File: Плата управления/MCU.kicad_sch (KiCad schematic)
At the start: 1 part, among them U5 STM32F071V8Tx

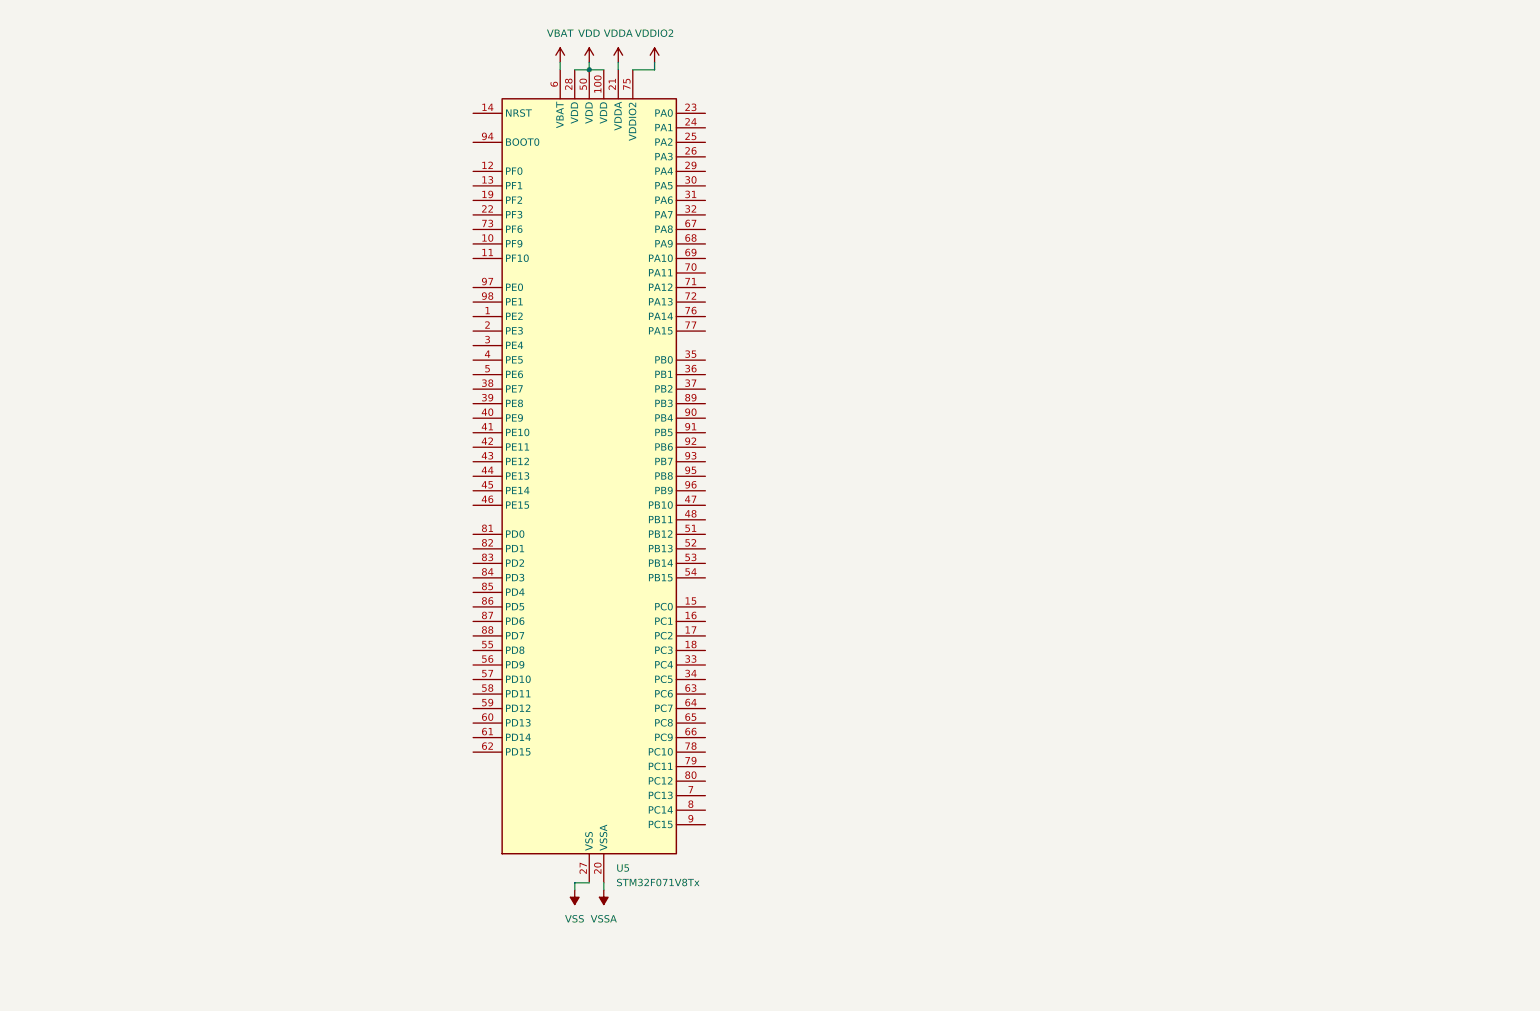
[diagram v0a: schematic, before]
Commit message: Добавил питание MCU и кварц на 8Мгц
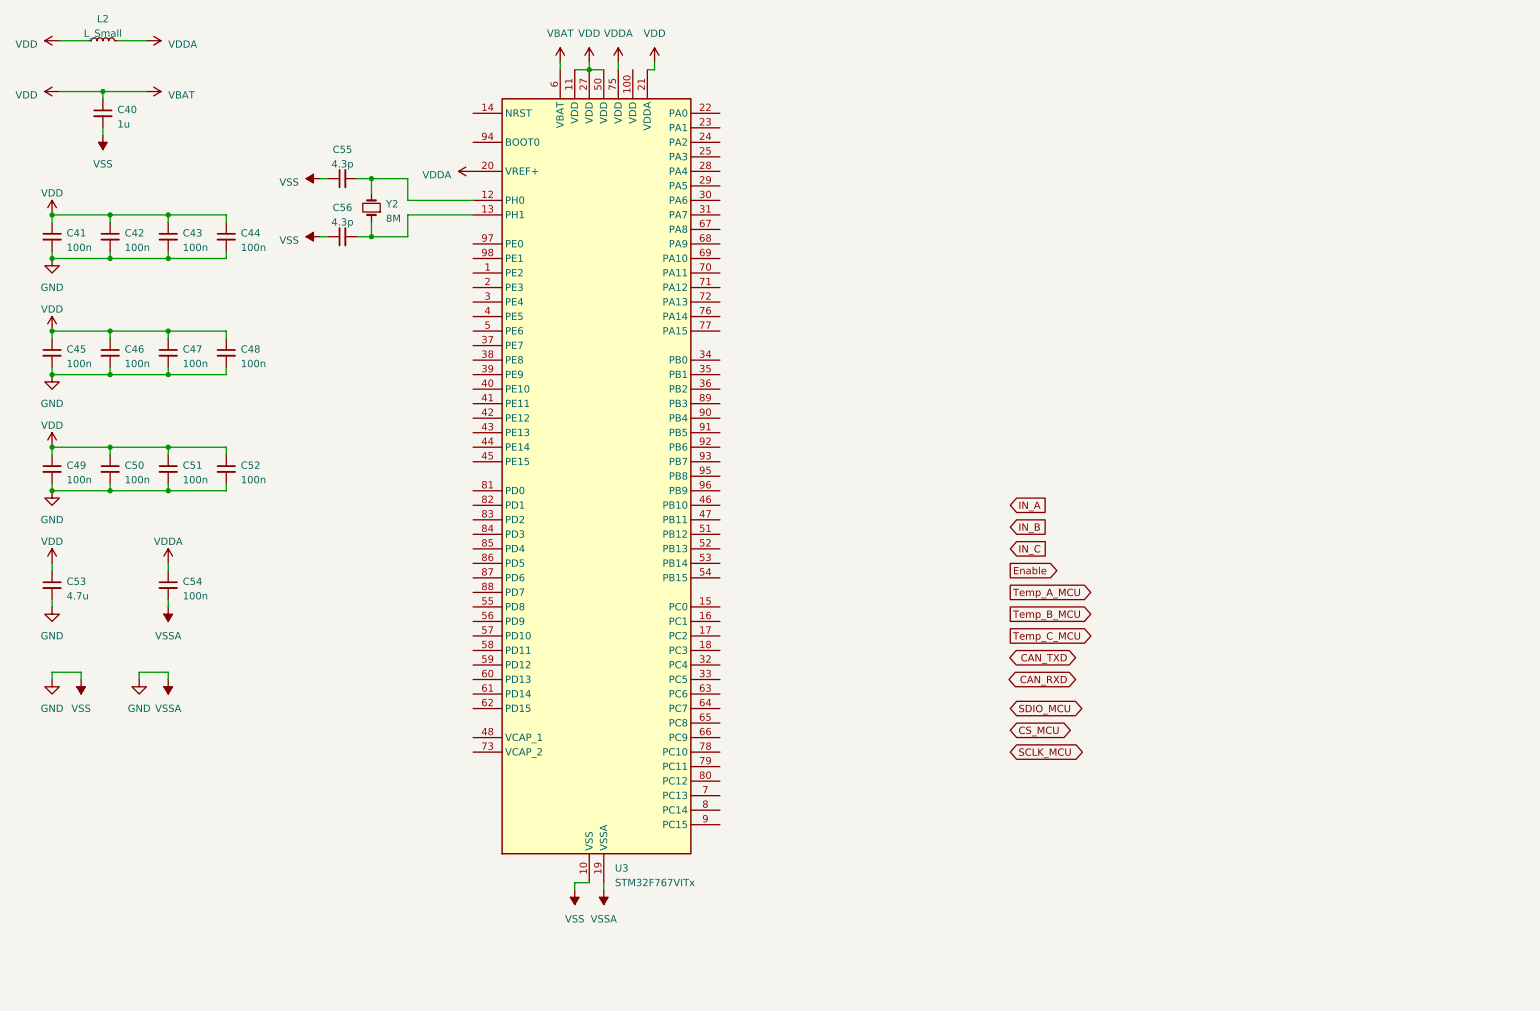
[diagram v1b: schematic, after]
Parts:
- removed U5: STM32F071V8Tx, Package_QFP:LQFP-100_14x14mm_P0.5mm, symbol MCU_ST_STM32F0:STM32F071V8Tx
- added C40: 1u, Capacitor_SMD:C_0603_1608Metric_Pad1.08x0.95mm_HandSolder, symbol Device:C_Small
- added C41, C42, C43, C44, C45, C46, C47, C48, C49, C50, C51, C52, C54: 100n, Capacitor_SMD:C_0603_1608Metric_Pad1.08x0.95mm_HandSolder, symbol Device:C_Small
- added C53: 4.7u, Capacitor_SMD:C_0603_1608Metric_Pad1.08x0.95mm_HandSolder, symbol Device:C_Small
- added C55, C56: 4.3p, Capacitor_SMD:C_0603_1608Metric_Pad1.08x0.95mm_HandSolder, symbol Device:C_Small
- added L2: L_Small, symbol Device:L_Small
- added U3: STM32F767VITx, Package_QFP:LQFP-100_14x14mm_P0.5mm, symbol MCU_ST_STM32F7:STM32F767VITx
- added Y2: 8M, symbol Device:Crystal_Small
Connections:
- net VDD: now also C40.1, C41.1, C42.1, C43.1, C44.1, C45.1, C46.1, C47.1, C48.1, C49.1, C50.1, C51.1, C52.1, C53.1, L2.1, U3.11 (VDD), U3.21 (VDDA), U3.27 (VDD), U3.50 (VDD), U3.6 (VBAT)
- net VDDA: now also C54.1, L2.2, U3.20 (VREF+), U3.75 (VDD)
- new net: C55.2, U3.12 (PH0), Y2.2
- new net: C56.2, U3.13 (PH1), Y2.1
- new net GND: C40.2, C41.2, C42.2, C43.2, C44.2, C45.2, C46.2, C47.2, C48.2, C49.2, C50.2, C51.2, C52.2, C53.2, C54.2, C55.1, C56.1, U3.10 (VSS), U3.19 (VSSA), U3.26 (VSS), U3.49 (VSS), U3.74 (VSS), U3.99 (VSS)

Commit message: Привел в порядок схему
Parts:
- Y1: renamed from Y2; footprint (none) -> Crystal:Crystal_SMD_MicroCrystal_CC1V-T1A-2Pin_8.0x3.7mm
- renumbered C55 to C19, C56 to C20, C41 to C21, C45 to C22, C49 to C23, C53 to C24, C40 to C25, C42 to C26, C46 to C27, C50 to C28, C43 to C29, C47 to C30, C51 to C31, C54 to C32, C44 to C33, C48 to C34, C52 to C35, L2 to L1, U3 to U4
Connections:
- net VDD renamed +3.3V
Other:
- moved on the sheet: C19, C20, C21, C22, C23, C24, C25, C26, C27, C28, C29, C30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

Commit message: Расставил драйвера
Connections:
- net +3.3V: now also U4.100 (VDD)
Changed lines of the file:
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@@
   (junction (at 242.57 69.85) (diameter 0) (color 0 0 0 0)
   )
+  (junction (at 81.28 24.13) (diameter 0) (color 0 0 0 0)
+  )
   (junction (at 242.57 97.79) (diameter 0) (color 0 0 0 0)
   )
@@
     (stroke (width 0) (type default))
   )
+  (wire (pts (xy 78.74 24.13) (xy 81.28 24.13))
+    (stroke (width 0) (type default))
+  )

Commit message: Добавил EEPROM
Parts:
- Y1: footprint Crystal:Crystal_SMD_MicroCrystal_CC1V-T1A-2Pin_8.0x3.7mm -> Crystal:Crystal_SMD_HC49-SD
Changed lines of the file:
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@@
       (effects (font (size 1.27 1.27)) (justify right))
     )
-    (property "Footprint" "Crystal:Crystal_SMD_MicroCrystal_CC1V-T1A-2Pin_8.0x3.7mm" (at 33.02 48.26 0)
+    (property "Footprint" "Crystal:Crystal_SMD_HC49-SD" (at 33.02 48.26 0)
       (effects (font (size 1.27 1.27)) hide)
     )

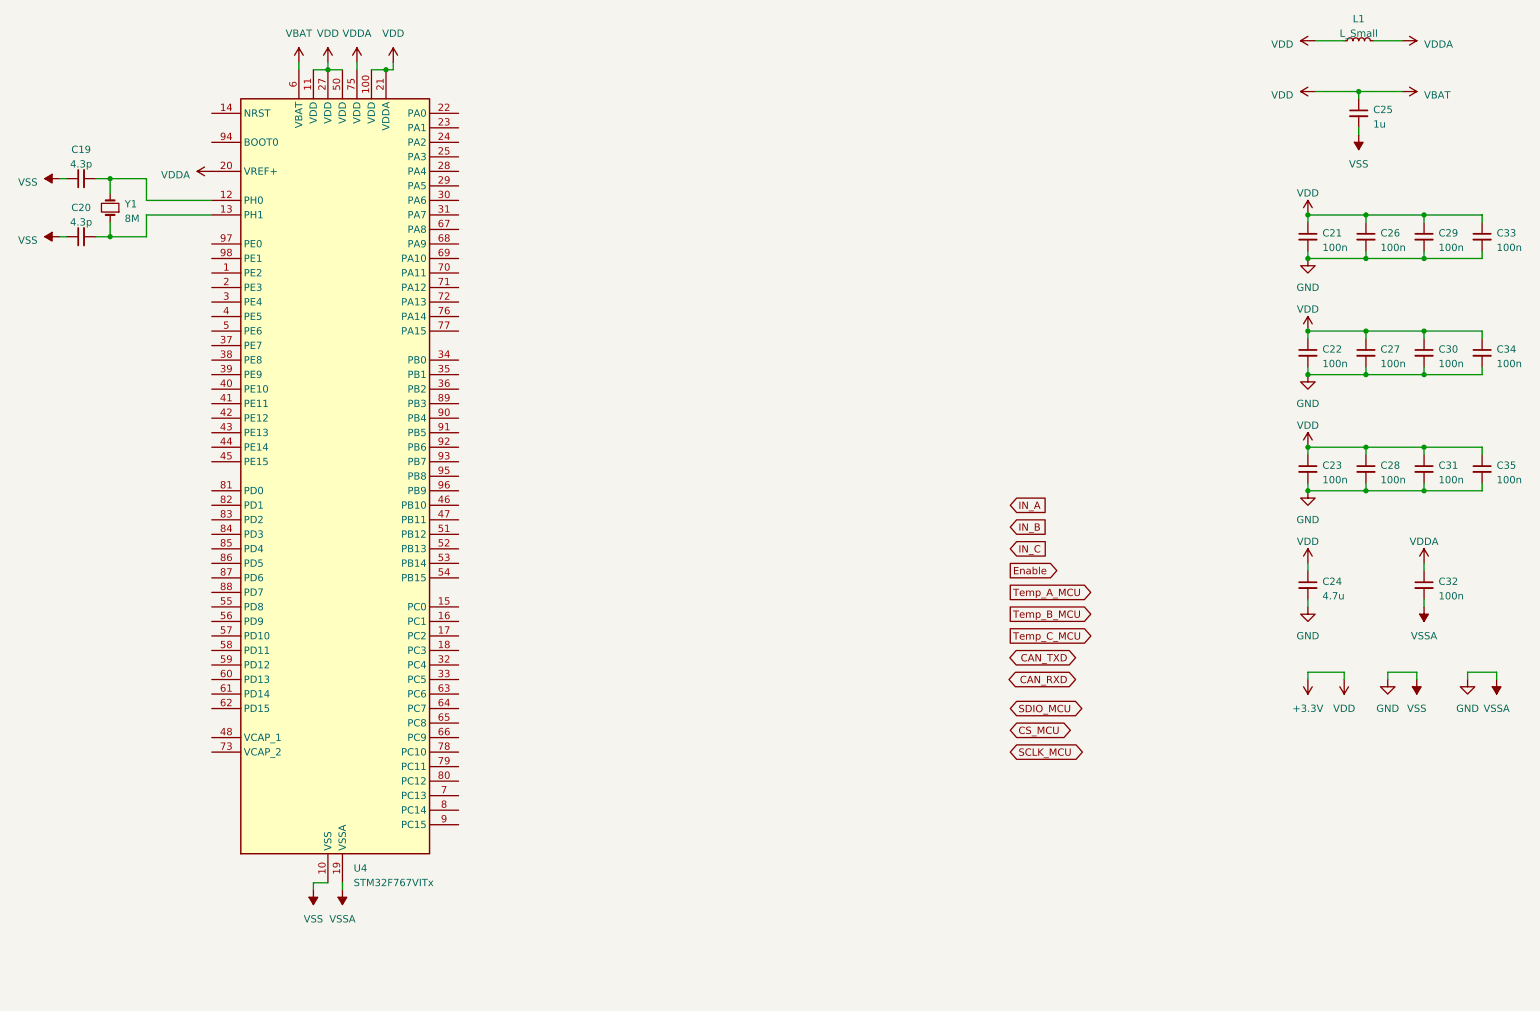
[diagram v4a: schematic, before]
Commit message: Добавил разъёмы под интерфейсы
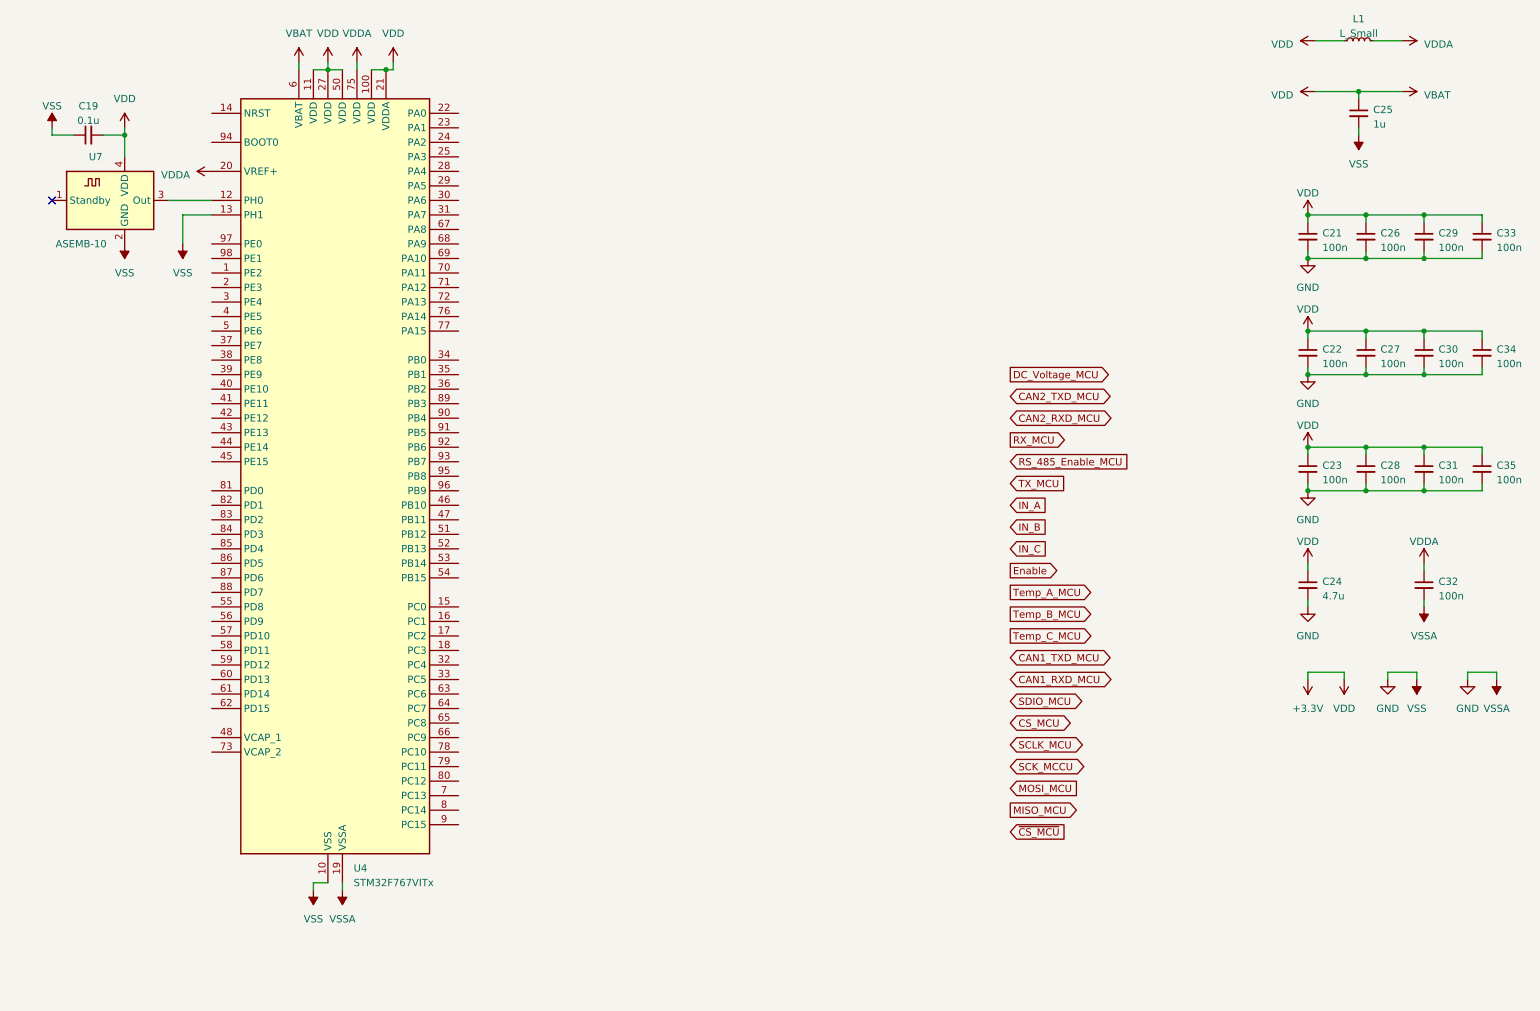
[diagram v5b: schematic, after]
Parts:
- removed C20: 4.3p, Capacitor_SMD:C_0603_1608Metric_Pad1.08x0.95mm_HandSolder, symbol Device:C_Small
- removed Y1: 8M, Crystal:Crystal_SMD_HC49-SD, symbol Device:Crystal_Small
- added U7: ASEMB-10, Oscillator:Oscillator_SMD_Abracon_ASE-4Pin_3.2x2.5mm_HandSoldering, symbol Oscillator:ASDMB-xxxMHz
- C19: value 4.3p -> 0.1u
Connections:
- net +3.3V: now also C19.2, U7.4 (VDD)
- net GND: now also U4.13 (PH1), U7.2 (GND)
- net at U4.12 (PH0): now also U7.3 (Out); no longer C19.2
- no-connect marks 0 -> 1

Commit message: Новый контур платы
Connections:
- net CAN1_RXD_MCU: now also U4.70 (PA11)
- net CAN1_TXD_MCU: now also U4.71 (PA12)
- net CAN2_RXD_MCU: now also U4.51 (PB12)
- net CAN2_TXD_MCU: now also U4.52 (PB13)
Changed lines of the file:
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@@
     (stroke (width 0) (type default))
+  )
+  (global_label "Analog_Input2" (shape input) (at 190.5 57.15 0) (fields_autoplaced)
+    (effects (font (size 1.27 1.27)) (justify left))
+    (property "Intersheetrefs" "${INTERSHEET_REFS}" (at 206.7896 57.15 0)
+      (effects (font (size 1.27 1.27)) (justify left) hide)
+    )
+  )
+  (global_label "Digital_input1" (shape input) (at 190.5 59.69 0) (fields_autoplaced)
+    (effects (font (size 1.27 1.27)) (justify left))
+    (property "Intersheetrefs" "${INTERSHEET_REFS}" (at 206.6083 59.69 0)
+      (effects (font (size 1.27 1.27)) (justify left) hide)
+    )
+  )
+  (global_label "Temp_Coil3_MCU" (shape output) (at 190.5 73.66 0) (fields_autoplaced)
+    (effects (font (size 1.27 1.27)) (justify left))
+    (property "Intersheetrefs" "${INTERSHEET_REFS}" (at 209.2693 73.66 0)
+      (effects (font (size 1.27 1.27)) (justify left) hide)
+    )
   )
   (global_label "MOSI_MCU" (shape input) (at 190.5 149.86 0) (fields_autoplaced)
@@
     )
   )
-  (global_label "CAN1_TXD_MCU" (shape bidirectional) (at 190.5 127 0) (fields_autoplaced)
+  (global_label "CAN1_TXD_MCU" (shape bidirectional) (at 93.98 62.23 0) (fields_autoplaced)
     (effects (font (size 1.27 1.27)) (justify left))
-    (property "Intersheetrefs" "${INTERSHEET_REFS}" (at 208.8499 127 0)
+    (property "Intersheetrefs" "${INTERSHEET_REFS}" (at 112.3299 62.23 0)
       (effects (font (size 1.27 1.27)) (justify left) hide)
     )
@@
     )
   )
+  (global_label "Digital_input2" (shape input) (at 190.5 62.23 0) (fields_autoplaced)
+    (effects (font (size 1.27 1.27)) (justify left))
+    (property "Intersheetrefs" "${INTERSHEET_REFS}" (at 206.6083 62.23 0)
+      (effects (font (size 1.27 1.27)) (justify left) hide)
+    )
+  )
   (global_label "IN_B" (shape input) (at 190.5 104.14 0) (fields_autoplaced)
     (effects (font (size 1.27 1.27)) (justify left))
     (property "Intersheetrefs" "${INTERSHEET_REFS}" (at 197.5787 104.14 0)
+      (effects (font (size 1.27 1.27)) (justify left) hide)
+    )
+  )
+  (global_label "Temp_Coil2_MCU" (shape output) (at 190.5 69.85 0) (fields_autoplaced)
+    (effects (font (size 1.27 1.27)) (justify left))
+    (property "Intersheetrefs" "${INTERSHEET_REFS}" (at 209.2693 69.85 0)
       (effects (font (size 1.27 1.27)) (justify left) hide)
     )
@@
     )
   )
-  (global_label "CAN1_RXD_MCU" (shape bidirectional) (at 190.5 130.81 0) (fields_autoplaced)
+  (global_label "CAN1_RXD_MCU" (shape bidirectional) (at 93.98 59.69 0) (fields_autoplaced)
     (effects (font (size 1.27 1.27)) (justify left))
-    (property "Intersheetrefs" "${INTERSHEET_REFS}" (at 209.1523 130.81 0)
+    (property "Intersheetrefs" "${INTERSHEET_REFS}" (at 112.6323 59.69 0)
       (effects (font (size 1.27 1.27)) (justify left) hide)
     )
   )
-  (global_label "CAN2_TXD_MCU" (shape bidirectional) (at 190.5 81.28 0) (fields_autoplaced)
+  (global_label "CAN2_TXD_MCU" (shape bidirectional) (at 93.98 107.95 0) (fields_autoplaced)
     (effects (font (size 1.27 1.27)) (justify left))
-    (property "Intersheetrefs" "${INTERSHEET_REFS}" (at 208.8499 81.28 0)
+    (property "Intersheetrefs" "${INTERSHEET_REFS}" (at 112.3299 107.95 0)
       (effects (font (size 1.27 1.27)) (justify left) hide)
     )
@@
     )
   )
+  (global_label "Temp_Coil1_MCU" (shape output) (at 190.5 66.04 0) (fields_autoplaced)
+    (effects (font (size 1.27 1.27)) (justify left))
+    (property "Intersheetrefs" "${INTERSHEET_REFS}" (at 209.2693 66.04 0)
+      (effects (font (size 1.27 1.27)) (justify left) hide)
+    )
+  )
   (global_label "Temp_A_MCU" (shape output) (at 190.5 115.57 0) (fields_autoplaced)
     (effects (font (size 1.27 1.27)) (justify left))
@@
     )
   )
-  (global_label "CAN2_RXD_MCU" (shape bidirectional) (at 190.5 85.09 0) (fields_autoplaced)
+  (global_label "CAN2_RXD_MCU" (shape bidirectional) (at 93.98 105.41 0) (fields_autoplaced)
     (effects (font (size 1.27 1.27)) (justify left))
-    (property "Intersheetrefs" "${INTERSHEET_REFS}" (at 209.1523 85.09 0)
+    (property "Intersheetrefs" "${INTERSHEET_REFS}" (at 112.6323 105.41 0)
       (effects (font (size 1.27 1.27)) (justify left) hide)
     )
@@
       (effects (font (size 1.27 1.27)) (justify left) hide)
     )
+  )
+  (global_label "Analog_Input1" (shape input) (at 190.5 54.61 0) (fields_autoplaced)
+    (effects (font (size 1.27 1.27)) (justify left))
+    (property "Intersheetrefs" "${INTERSHEET_REFS}" (at 206.7896 54.61 0)
+      (effects (font (size 1.27 1.27)) (justify left) hide)
+    )
